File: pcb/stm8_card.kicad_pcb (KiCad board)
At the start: 2 copper layers, 101.9 x 50.9 mm, 22 parts, among them J1 DEBUG HEADER, SW1 TL59AF100Q, SW2 TL59AF100Q, SW3 TL59AF100Q, SW4 TL3302AF260QG, U1 ER-OLED0.91-7, U2 STM8S103F3

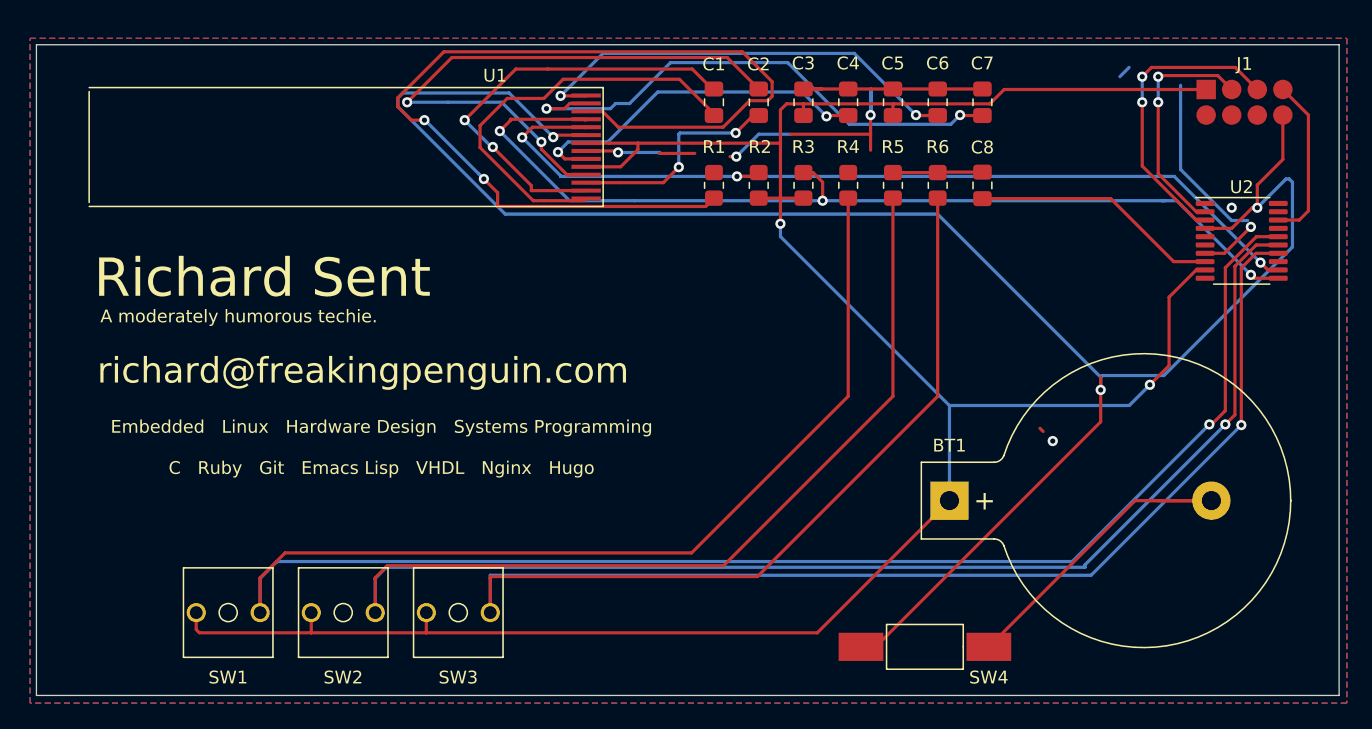
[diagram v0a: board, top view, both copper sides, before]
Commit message: small edits, still need to correct cap issue also add led + res
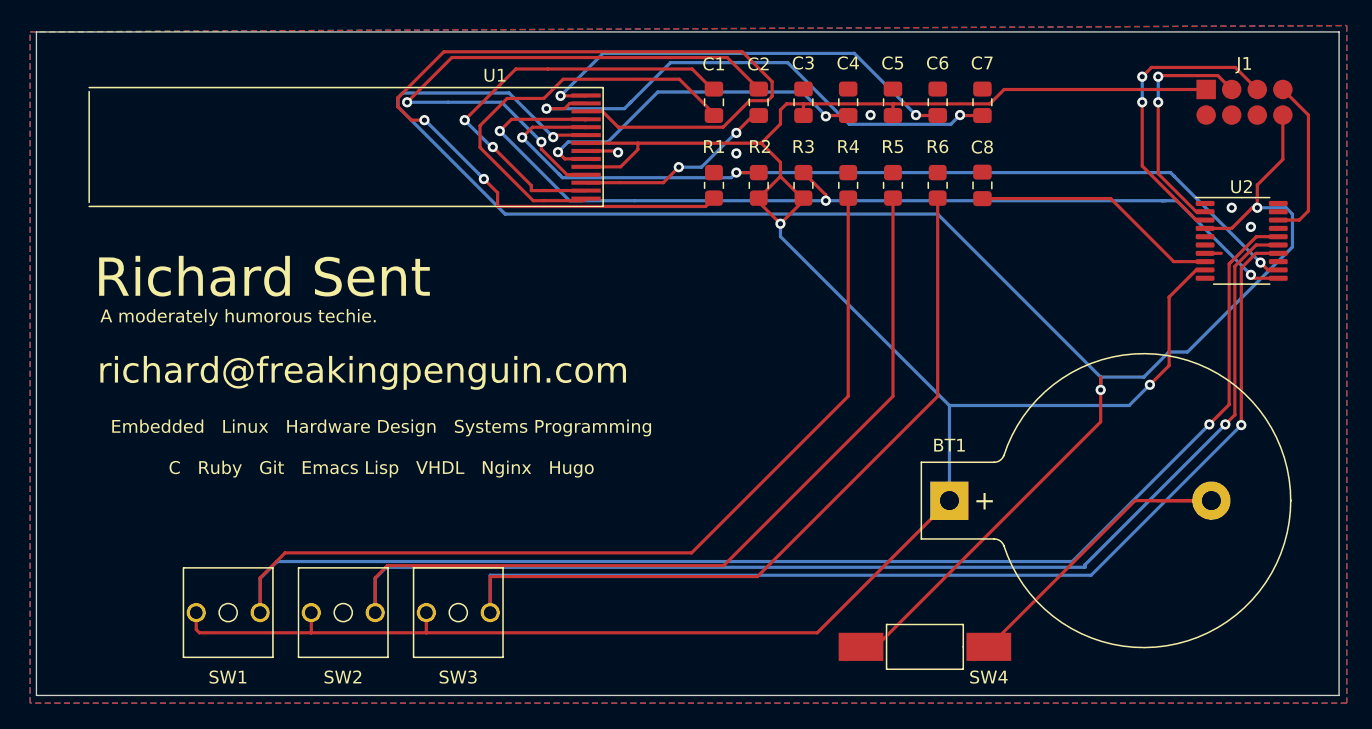
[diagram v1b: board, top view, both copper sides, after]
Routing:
- net GND: track 100.3 -> 35.5 mm, vias 6 -> 5
- net NRST: track 152.3 -> 148.9 mm
- net 3v3: track 191.0 -> 193.9 mm
- net Net-(C2-Pad1): track 17.2 -> 15.7 mm
- net SCL: track 71.0 -> 71.5 mm
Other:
- board size 101.9 x 50.9 mm -> 101.9 x 51.9 mm

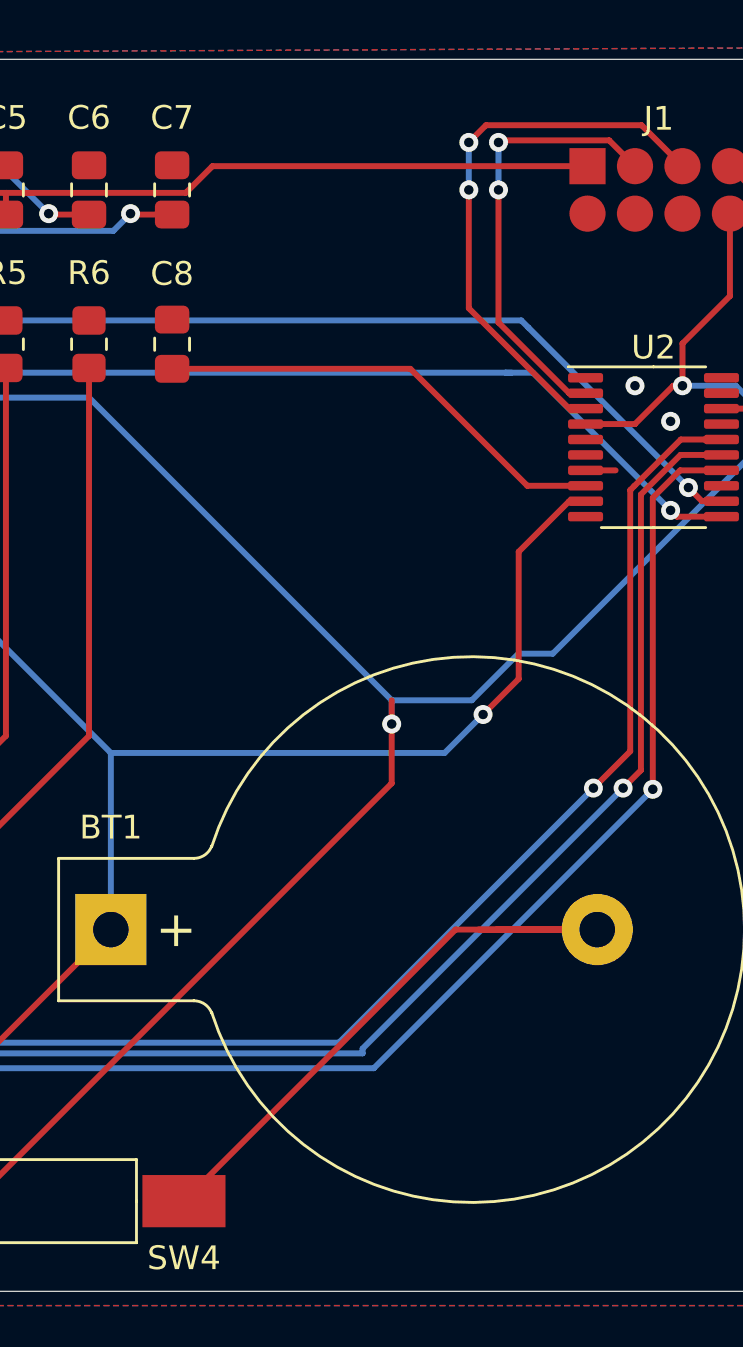
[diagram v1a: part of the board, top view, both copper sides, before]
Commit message: pcb improved pcb + added led, res, and mcu cap
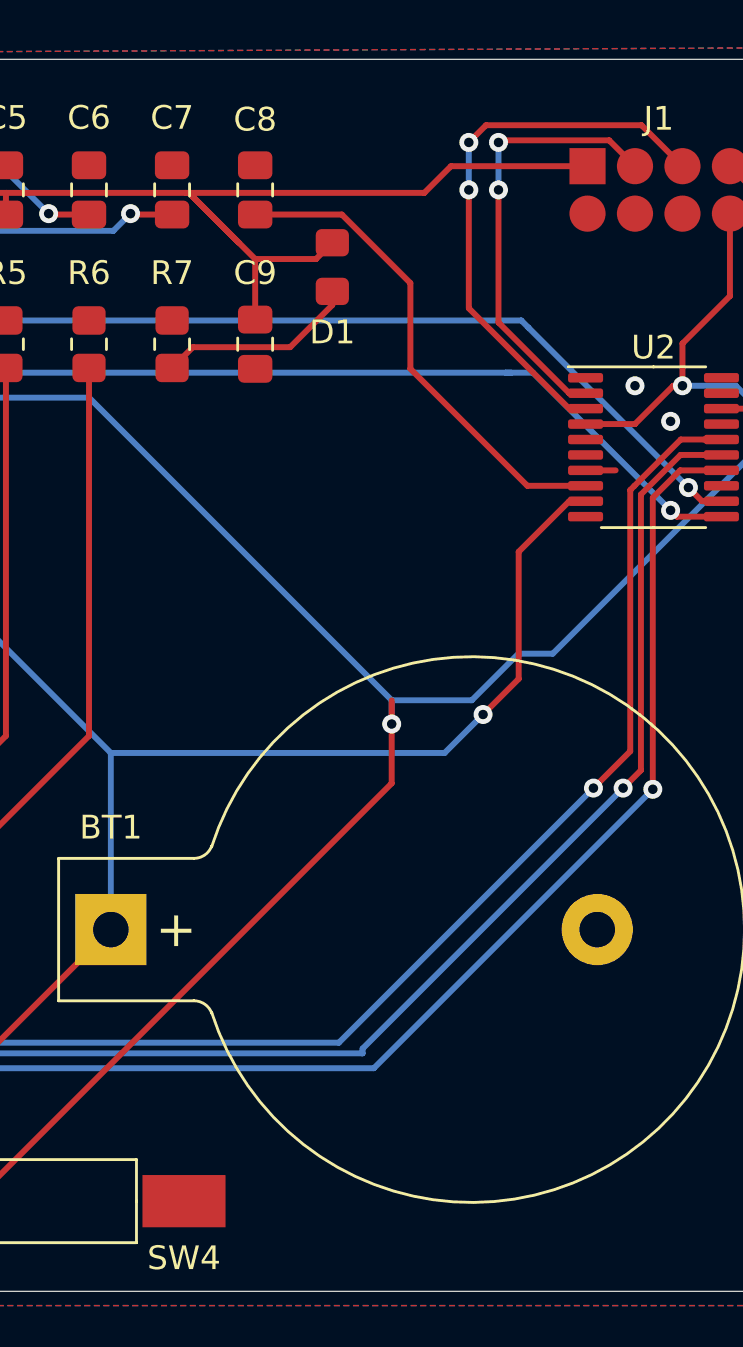
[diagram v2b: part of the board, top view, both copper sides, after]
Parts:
- added C9: 1uf, Capacitor_SMD:C_0805_2012Metric_Pad1.18x1.45mm_HandSolder, F.Cu at (255.0, 112.5)
- added D1: LED, stm8_card:LED_0805_2012Metric_Pad1.15x1.40mm_HandSolder, F.Cu at (258.2, 109.2)
- added R7: 470, Resistor_SMD:R_0805_2012Metric_Pad1.20x1.40mm_HandSolder, F.Cu at (251.5, 112.5)
- moved C8 7.38 mm to (255.0, 106.0)
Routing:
- net GND: track 35.5 -> 3.98 mm
- net 3v3: track 193.9 -> 206.8 mm
- net Net-(D1-Pad1): track 0.00 -> 8.42 mm
- net Net-(C8-Pad1): track 19.5 -> 20.8 mm

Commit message: pcb improvements
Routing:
- net NRST: track 148.9 -> 147.9 mm
- net 3v3: track 206.8 -> 207.5 mm
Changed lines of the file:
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@@
     (thickness 1.6)
     (drawings 10)
-    (tracks 317)
+    (tracks 319)
     (zones 0)
     (modules 25)
@@
     (tags "LED handsolder")
     (attr smd)
-    (fp_text reference D1 (at -2.75 0 180) (layer F.SilkS)
+    (fp_text reference D1 (at 3 0 180) (layer F.SilkS)
       (effects (font (size 1 1) (thickness 0.15)))
     )
@@
   (via (at 235.7 115.5) (size 0.8) (drill 0.4) (layers F.Cu B.Cu) (net 2))
   (segment (start 248.92 129.72) (end 235.7 116.5) (width 0.25) (layer B.Cu) (net 2))
-  (segment (start 264.6 128.1) (end 266.1 126.6) (width 0.25) (layer F.Cu) (net 2))
-  (segment (start 268.228942 119.115) (end 268.9175 119.115) (width 0.25) (layer F.Cu) (net 2))
-  (segment (start 266.1 121.243942) (end 268.228942 119.115) (width 0.25) (layer F.Cu) (net 2))
-  (segment (start 266.1 126.6) (end 266.1 121.243942) (width 0.25) (layer F.Cu) (net 2))
   (segment (start 224.55 109.7) (end 224.55 109.2) (width 0.25) (layer F.Cu) (net 2))
   (segment (start 220.5 111.05) (end 223.2 111.05) (width 0.25) (layer F.Cu) (net 2))
@@
   (segment (start 252.294095 106.205905) (end 254.31319 108.225) (width 0.25) (layer F.Cu) (net 2))
   (segment (start 252.21318 106.12499) (end 252.294095 106.205905) (width 0.25) (layer F.Cu) (net 2))
-  (segment (start 257.56319 108.91181) (end 258.25 108.225) (width 0.25) (layer F.Cu) (net 2))
-  (segment (start 255 108.91181) (end 257.56319 108.91181) (width 0.25) (layer F.Cu) (net 2))
   (segment (start 252.21318 106.12499) (end 262.12501 106.12499) (width 0.25) (layer F.Cu) (net 2))
   (segment (start 263.25 105) (end 269 105) (width 0.25) (layer F.Cu) (net 2))
   (segment (start 262.12501 106.12499) (end 263.25 105) (width 0.25) (layer F.Cu) (net 2))
+  (segment (start 255.68681 108.225) (end 255 108.91181) (width 0.25) (layer F.Cu) (net 2))
+  (segment (start 258.25 108.225) (end 255.68681 108.225) (width 0.25) (layer F.Cu) (net 2))
+  (segment (start 266.1 126.6) (end 264.6 128.1) (width 0.25) (layer F.Cu) (net 2))
+  (segment (start 266.1 120) (end 266.1 126.6) (width 0.25) (layer F.Cu) (net 2))
+  (segment (start 266.985 119.115) (end 266.1 120) (width 0.25) (layer F.Cu) (net 2))
+  (segment (start 268.9175 119.115) (end 266.985 119.115) (width 0.25) (layer F.Cu) (net 2))
   (segment (start 230.5 104.9625) (end 230.3625 104.9625) (width 0.25) (layer F.Cu) (net 3))
   (segment (start 230.3625 104.9625) (end 228.8 103.4) (width 0.25) (layer F.Cu) (net 3))
@@
   (segment (start 224 106) (end 223.9 106.1) (width 0.25) (layer B.Cu) (net 9))
   (segment (start 227.1 102.9) (end 224 106) (width 0.25) (layer B.Cu) (net 9))
-  (segment (start 266.465 118.465) (end 268.9175 118.465) (width 0.25) (layer F.Cu) (net 10))
-  (segment (start 261.5375 113.5375) (end 266.465 118.465) (width 0.25) (layer F.Cu) (net 10))
-  (segment (start 258.65069 107.0375) (end 255 107.0375) (width 0.25) (layer F.Cu) (net 10))
-  (segment (start 261.5375 109.92431) (end 258.65069 107.0375) (width 0.25) (layer F.Cu) (net 10))
-  (segment (start 261.5375 113.5375) (end 261.5375 109.92431) (width 0.25) (layer F.Cu) (net 10))
+  (segment (start 261.5375 113.0375) (end 266.965 118.465) (width 0.25) (layer F.Cu) (net 10))
+  (segment (start 261.5375 109.92431) (end 261.5375 113.0375) (width 0.25) (layer F.Cu) (net 10))
+  (segment (start 258.65069 107.0375) (end 261.5375 109.92431) (width 0.25) (layer F.Cu) (net 10))
+  (segment (start 266.965 118.465) (end 268.9175 118.465) (width 0.25) (layer F.Cu) (net 10))
+  (segment (start 255 107.0375) (end 258.65069 107.0375) (width 0.25) (layer F.Cu) (net 10))
   (segment (start 265.337001 103.912999) (end 265.25 104) (width 0.25) (layer F.Cu) (net 11))
   (segment (start 269.912999 103.912999) (end 265.337001 103.912999) (width 0.25) (layer F.Cu) (net 11))
@@
   (via (at 265.25 106) (size 0.8) (drill 0.4) (layers F.Cu B.Cu) (net 11))
   (segment (start 265.25 104) (end 265.25 106) (width 0.25) (layer B.Cu) (net 11))
-  (segment (start 268.228942 114.565) (end 268.9175 114.565) (width 0.25) (layer F.Cu) (net 11))
-  (segment (start 265.25 111.586058) (end 268.228942 114.565) (width 0.25) (layer F.Cu) (net 11))
   (segment (start 265.25 106) (end 265.25 111.586058) (width 0.25) (layer F.Cu) (net 11))
+  (segment (start 265.25 111.635) (end 265.25 111.586058) (width 0.25) (layer F.Cu) (net 11))
+  (segment (start 268.18 114.565) (end 265.25 111.635) (width 0.25) (layer F.Cu) (net 11))
+  (segment (start 268.9175 114.565) (end 268.18 114.565) (width 0.25) (layer F.Cu) (net 11))
   (via (at 264 104) (size 0.8) (drill 0.4) (layers F.Cu B.Cu) (net 12))
   (segment (start 264.725001 103.274999) (end 264 104) (width 0.25) (layer F.Cu) (net 12))
@@
   (via (at 264 106) (size 0.8) (drill 0.4) (layers F.Cu B.Cu) (net 12))
   (segment (start 264 104) (end 264 106) (width 0.25) (layer B.Cu) (net 12))
-  (segment (start 268.228942 115.215) (end 268.9175 115.215) (width 0.25) (layer F.Cu) (net 12))
-  (segment (start 264 110.986058) (end 268.228942 115.215) (width 0.25) (layer F.Cu) (net 12))
   (segment (start 264 106) (end 264 110.986058) (width 0.25) (layer F.Cu) (net 12))
+  (segment (start 268.9175 115.215) (end 267.715 115.215) (width 0.25) (layer F.Cu) (net 12))
+  (segment (start 264 111.5) (end 264 110.986058) (width 0.25) (layer F.Cu) (net 12))
+  (segment (start 267.715 115.215) (end 264 111.5) (width 0.25) (layer F.Cu) (net 12))
   (segment (start 274.6425 115.215) (end 276.285 115.215) (width 0.25) (layer F.Cu) (net 13))
   (segment (start 276.285 115.215) (end 277 114.5) (width 0.25) (layer F.Cu) (net 13))
@@
   (via (at 273 114.25) (size 0.8) (drill 0.4) (layers F.Cu B.Cu) (net 14))
   (segment (start 242 148.6) (end 243.15 148.6) (width 0.25) (layer F.Cu) (net 14))
-  (segment (start 260.75 131) (end 260.75 127.5) (width 0.25) (layer F.Cu) (net 14))
   (segment (start 243.15 148.6) (end 260.75 131) (width 0.25) (layer F.Cu) (net 14))
   (segment (start 272.61359 114.25) (end 273 114.25) (width 0.25) (layer F.Cu) (net 14))
@@
   (segment (start 273 112.471058) (end 275 110.471058) (width 0.25) (layer F.Cu) (net 14))
   (segment (start 273 114.25) (end 273 112.471058) (width 0.25) (layer F.Cu) (net 14))
-  (segment (start 260.75 127.5) (end 260.75 128.5) (width 0.25) (layer B.Cu) (net 14))
   (segment (start 273 114.25) (end 275.25 114.25) (width 0.25) (layer B.Cu) (net 14))
   (segment (start 275.75 114.75) (end 275.75 117.323002) (width 0.25) (layer B.Cu) (net 14))
@@
   (segment (start 260.75 127.5) (end 264.126998 127.5) (width 0.25) (layer B.Cu) (net 14))
   (segment (start 267.536501 125.536501) (end 275.75 117.323002) (width 0.25) (layer B.Cu) (net 14))
+  (segment (start 260.75 127.5) (end 260.75 128.5) (width 0.25) (layer B.Cu) (net 14))
+  (segment (start 260.75 131) (end 260.75 128.5) (width 0.25) (layer F.Cu) (net 14))
   (segment (start 221.775002 106.71) (end 220.5 106.71) (width 0.25) (layer F.Cu) (net 17))
   (segment (start 223.015012 107.95001) (end 221.775002 106.71) (width 0.25) (layer F.Cu) (net 17))

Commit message: pcb AESTHETIC
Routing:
- net btn2: track 141.4 -> 138.8 mm
- net btn1: track 156.4 -> 154.5 mm
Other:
- board text added: "Embedded | Linux | Hardware Design | Systems Programming C | Ruby | Emacs Lisp | VHDL | Git | Nginx | Hugo"
- board text removed: "Embedded Linux Hardware Design Systems Programming C Ruby Git Emacs Lisp VHDL Nginx Hugo"
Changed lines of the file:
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@@
     (thickness 1.6)
     (drawings 10)
-    (tracks 319)
+    (tracks 318)
     (zones 0)
     (modules 25)
@@
       (net 1 GND))
   )
-  (gr_text "Embedded   Linux   Hardware Design   Systems Programming\n\nC   Ruby   Git   Emacs Lisp   VHDL   Nginx   Hugo" (at 204.5 133) (layer F.SilkS)
+  (gr_text "Embedded | Linux | Hardware Design | Systems Programming\n\nC | Ruby | Emacs Lisp | VHDL | Git | Nginx | Hugo" (at 204.5 133) (layer F.SilkS)
     (effects (font (size 1 1) (thickness 0.15)))
   )
@@
   (segment (start 273.91859 116.515) (end 274.6425 116.515) (width 0.25) (layer F.Cu) (net 20))
   (via (at 269.25 131.2) (size 0.8) (drill 0.4) (layers F.Cu B.Cu) (net 20))
-  (segment (start 195 143.2) (end 196.95 141.25) (width 0.25) (layer F.Cu) (net 20))
-  (segment (start 196.95 141.25) (end 228.75 141.25) (width 0.25) (layer F.Cu) (net 20))
-  (segment (start 241 129) (end 241 113.5) (width 0.25) (layer F.Cu) (net 20))
-  (segment (start 228.75 141.25) (end 241 129) (width 0.25) (layer F.Cu) (net 20))
-  (segment (start 195 145.92) (end 195 143.2) (width 0.25) (layer F.Cu) (net 20))
   (segment (start 258.525011 141.924989) (end 269.25 131.2) (width 0.25) (layer B.Cu) (net 20))
   (segment (start 196.275011 141.924989) (end 258.525011 141.924989) (width 0.25) (layer B.Cu) (net 20))
@@
   (segment (start 270.79999 129.65001) (end 270.79999 118.644188) (width 0.25) (layer F.Cu) (net 20))
   (segment (start 272.929178 116.515) (end 270.972089 118.472089) (width 0.25) (layer F.Cu) (net 20))
+  (segment (start 241 113.5) (end 241 125) (width 0.25) (layer F.Cu) (net 20))
+  (segment (start 241 125) (end 229 137) (width 0.25) (layer F.Cu) (net 20))
+  (segment (start 229 137) (end 198 137) (width 0.25) (layer F.Cu) (net 20))
+  (segment (start 195 140) (end 195 145.92) (width 0.25) (layer F.Cu) (net 20))
+  (segment (start 198 137) (end 195 140) (width 0.25) (layer F.Cu) (net 20))
   (segment (start 273.905 117.165) (end 274.6425 117.165) (width 0.25) (layer F.Cu) (net 21))
-  (segment (start 204.95 142.25) (end 231.25 142.25) (width 0.25) (layer F.Cu) (net 21))
   (segment (start 204.825001 142.374999) (end 259.525001 142.374999) (width 0.25) (layer B.Cu) (net 21))
-  (segment (start 231.25 142.25) (end 244.5 129) (width 0.25) (layer F.Cu) (net 21))
-  (segment (start 204 143.2) (end 204.95 142.25) (width 0.25) (layer F.Cu) (net 21))
-  (segment (start 244.5 129) (end 244.5 113.5) (width 0.25) (layer F.Cu) (net 21))
   (via (at 270.5 131.2) (size 0.8) (drill 0.4) (layers F.Cu B.Cu) (net 21))
-  (segment (start 204 145.92) (end 204 143.2) (width 0.25) (layer F.Cu) (net 21))
   (segment (start 204.825001 142.374999) (end 204.825001 142.424999) (width 0.25) (layer B.Cu) (net 21))
   (segment (start 204 143.25) (end 204 145.92) (width 0.25) (layer B.Cu) (net 21))
@@
   (segment (start 271.25 130.45) (end 270.5 131.2) (width 0.25) (layer F.Cu) (net 21))
   (segment (start 271.25 118.830588) (end 271.25 130.45) (width 0.25) (layer F.Cu) (net 21))
-  (segment (start 248 129) (end 248 113.5) (width 0.25) (layer F.Cu) (net 22))
-  (segment (start 233.9 143.1) (end 248 129) (width 0.25) (layer F.Cu) (net 22))
-  (segment (start 272.901998 117.815) (end 271.75 118.966998) (width 0.25) (layer F.Cu) (net 22))
-  (segment (start 274.6425 117.815) (end 272.901998 117.815) (width 0.25) (layer F.Cu) (net 22))
+  (segment (start 244.5 125.5) (end 244.5 113.5) (width 0.25) (layer F.Cu) (net 21))
+  (segment (start 229.5 140.5) (end 244.5 125.5) (width 0.25) (layer F.Cu) (net 21))
+  (segment (start 206.5 140.5) (end 229.5 140.5) (width 0.25) (layer F.Cu) (net 21))
+  (segment (start 204 143) (end 206.5 140.5) (width 0.25) (layer F.Cu) (net 21))
+  (segment (start 204 145.92) (end 204 143) (width 0.25) (layer F.Cu) (net 21))
   (via (at 271.75 131.25) (size 0.8) (drill 0.4) (layers F.Cu B.Cu) (net 22))
+  (segment (start 213 143) (end 213 145.92) (width 0.25) (layer B.Cu) (net 22))
+  (segment (start 260 143) (end 213 143) (width 0.25) (layer B.Cu) (net 22))
   (segment (start 271.75 118.966998) (end 271.75 131.25) (width 0.25) (layer F.Cu) (net 22))
   (segment (start 271.75 131.25) (end 260 143) (width 0.25) (layer B.Cu) (net 22))
-  (segment (start 260 143) (end 213 143) (width 0.25) (layer B.Cu) (net 22))
-  (segment (start 213 143) (end 213 145.92) (width 0.25) (layer B.Cu) (net 22))
-  (segment (start 213 143.2) (end 213.1 143.1) (width 0.25) (layer F.Cu) (net 22))
-  (segment (start 213.1 143.1) (end 233.9 143.1) (width 0.25) (layer F.Cu) (net 22))
-  (segment (start 213 145.92) (end 213 143.2) (width 0.25) (layer F.Cu) (net 22))
-  (segment (start 213 143.1) (end 213.1 143.1) (width 0.25) (layer F.Cu) (net 22))
+  (segment (start 274.6425 117.815) (end 272.901998 117.815) (width 0.25) (layer F.Cu) (net 22))
+  (segment (start 272.901998 117.815) (end 271.75 118.966998) (width 0.25) (layer F.Cu) (net 22))
+  (segment (start 230 144) (end 248 126) (width 0.25) (layer F.Cu) (net 22))
+  (segment (start 248 126) (end 248 113.5) (width 0.25) (layer F.Cu) (net 22))
+  (segment (start 213.5 144) (end 230 144) (width 0.25) (layer F.Cu) (net 22))
+  (segment (start 213 144.5) (end 213.5 144) (width 0.25) (layer F.Cu) (net 22))
+  (segment (start 213 145.92) (end 213 144.5) (width 0.25) (layer F.Cu) (net 22))
   (segment (start 252.37501 112.62499) (end 251.5 113.5) (width 0.25) (layer F.Cu) (net 31))
   (segment (start 256.47501 112.62499) (end 252.37501 112.62499) (width 0.25) (layer F.Cu) (net 31))
